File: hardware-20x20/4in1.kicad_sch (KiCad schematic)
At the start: 29 parts, among them J1 SM08B-SRSS-TB, U12 INA186A3IDCKR, U13 LMR54406DBVR, U14 FTC160808S4R7MBCA, U15 TLV76733DRVR

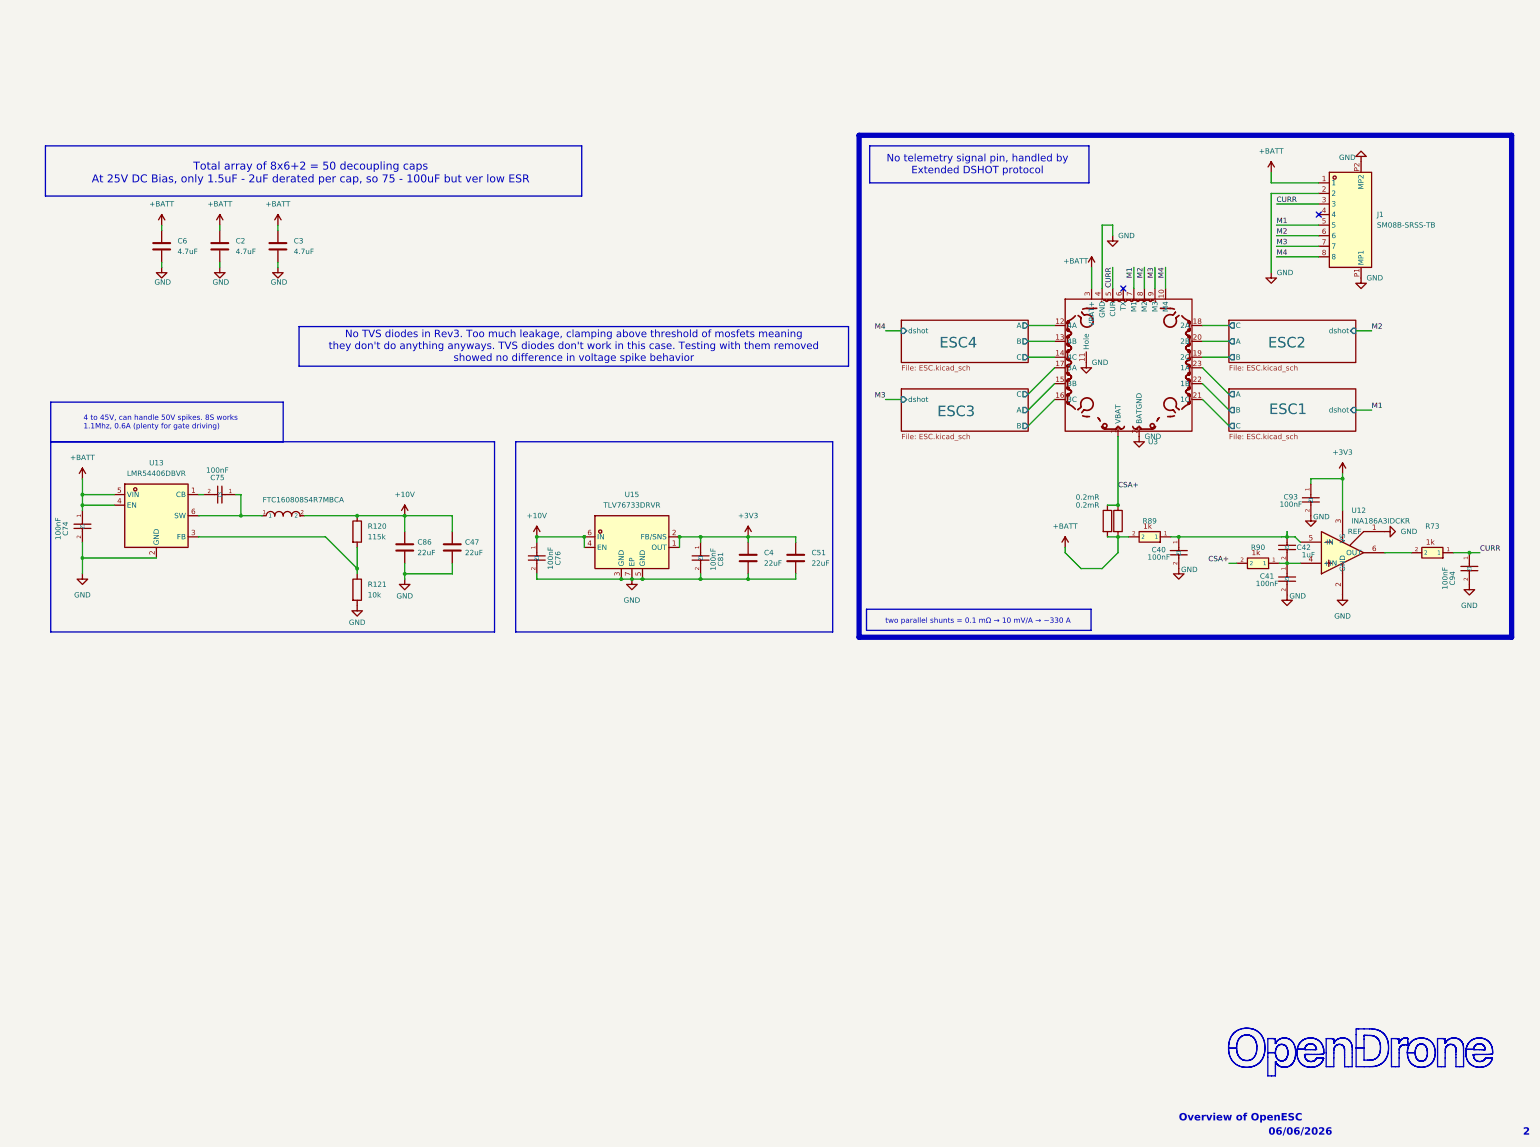
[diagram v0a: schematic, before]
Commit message: Match the schematic to the board and redraw the U3 block
Schematic (edited in KiCad 10, netlist diffed against the original):
- remove the current-sense circuit (U12, Rsense1/2, R89, R90, C40-C42,
  C94, R73) and wire the battery pad straight to +BATT
- add J2, the 8-pad castellated strip (+BATT, GND, CURR, unused, M1-M4)
- U3 board block: drop pins 3-11 that no longer have pads and redraw it as
  the real outline (chamfered top strip, battery tab, 4 mounting holes)
- remove the orphaned labels and wires left by those pins

Docs: README and design notes updated for the schematic changes, the
castellation fix and the current ERC and parity results.

Co-Authored-By: Claude Sonnet 5.5 <noreply@anthropic.com>
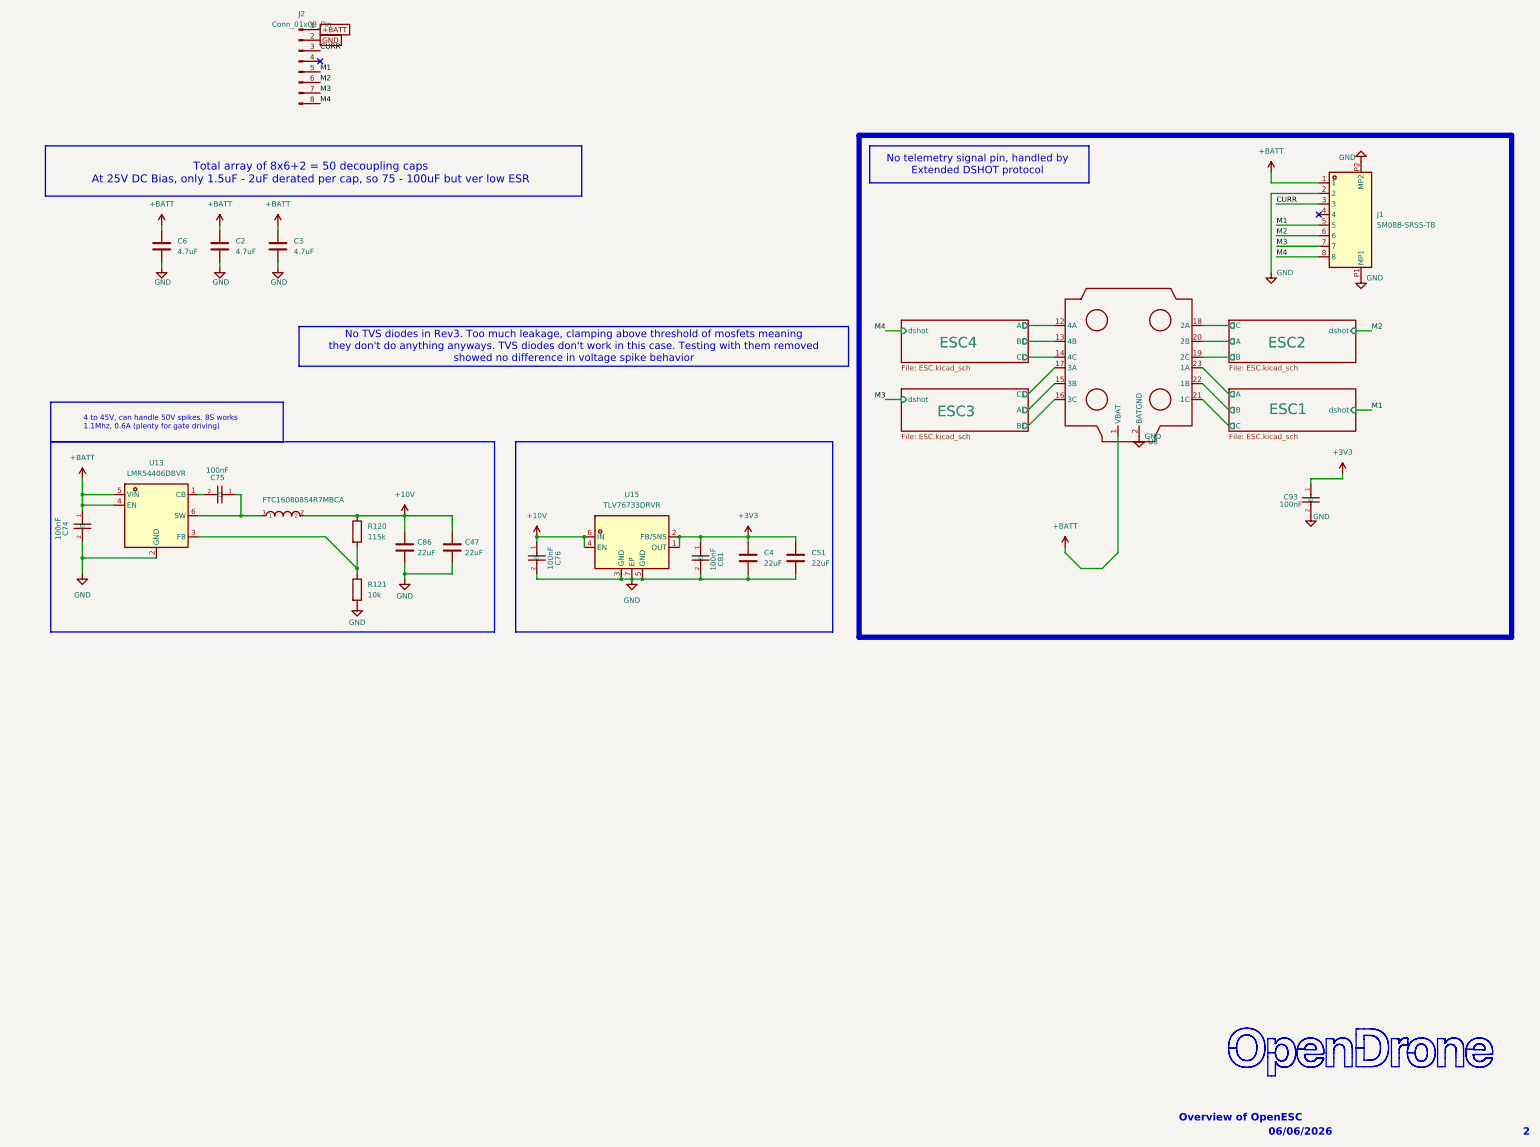
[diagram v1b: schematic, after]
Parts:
- removed C40, C41: 100nF, Capacitor_SMD:C_0402_WIDE, symbol ESCLibrary:GRM033R61C104KE84D
- removed C42: 1uF, 4in1ESC-30x30:C_0402_1005Metric, symbol ESCLibrary:GRM033R61C104KE84D
- removed C94: 100nF, Capacitor_SMD:C_0201_0603Metric, symbol components:GRM033R61C104KE84D
- removed R73, R89, R90: 1k, Capacitor_SMD:C_0201_0603Metric, symbol components:0201_1kR
- removed Rsense1, Rsense2: 0.2mR, Resistor_SMD:R_2512_6332Metric, symbol Device:R
- removed U12: INA186A3IDCKR, 4in1ESC-30x30:SOT-363_SC-70-6, symbol components:INA186A3IDCKR
- added J2: Conn_01x08_Pin, OpenESC-alt:Castellated_8x1.50, symbol Connector:Conn_01x08_Pin
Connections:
- net CSA+ is gone; now on net +BATT: U3.1 (VBAT)
- net +BATT: now also J2.1 (Pin_1); no longer U3.3 (VBAT+)
- net CURR: now also J2.3 (Pin_3); no longer U3.5 (CUR)
- net GND: now also J2.2 (Pin_2); no longer U3.11 (Hole), U3.4 (GND)
- net M1: now also J2.5 (Pin_5); no longer U3.7 (M1)
- net M2: now also J2.6 (Pin_6); no longer U3.8 (M2)
- net M3: now also J2.7 (Pin_7); no longer U3.9 (M3)
- net M4: now also J2.8 (Pin_8); no longer U3.10 (M4)
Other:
- note removed: "two parallel shunts = 0.1 mΩ → 10 mV/A → ~330 A"
